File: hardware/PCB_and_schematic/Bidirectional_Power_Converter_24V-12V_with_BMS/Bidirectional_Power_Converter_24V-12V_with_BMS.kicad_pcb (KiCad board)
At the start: 2 copper layers, 100 x 100 mm, 8 parts, among them J1 AC_IN, J2 DC_OUT, Q1 IRF540N, Q2 IRF540N, Q3 IRF540N, Q4 IRF540N, U1 LT4320xDD-1

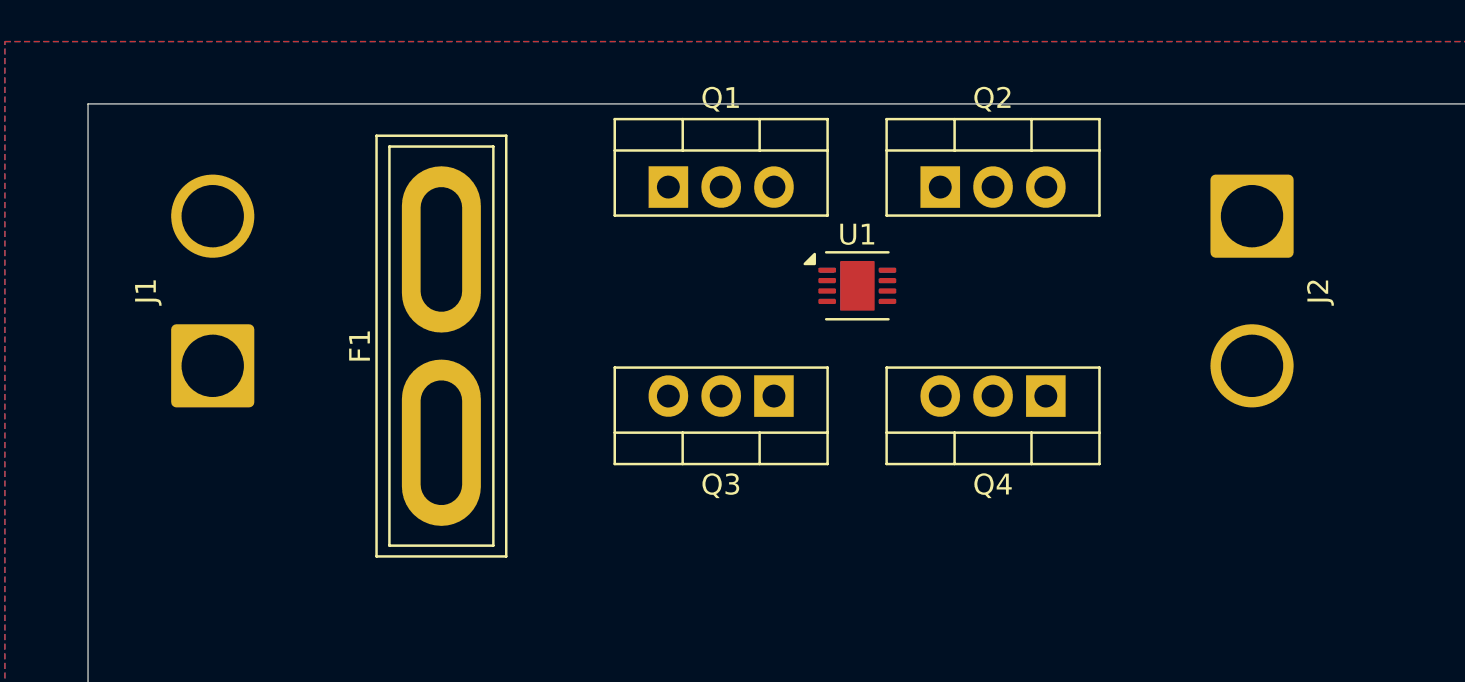
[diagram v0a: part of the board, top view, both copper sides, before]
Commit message: Drawning schematic for buck/boost converter
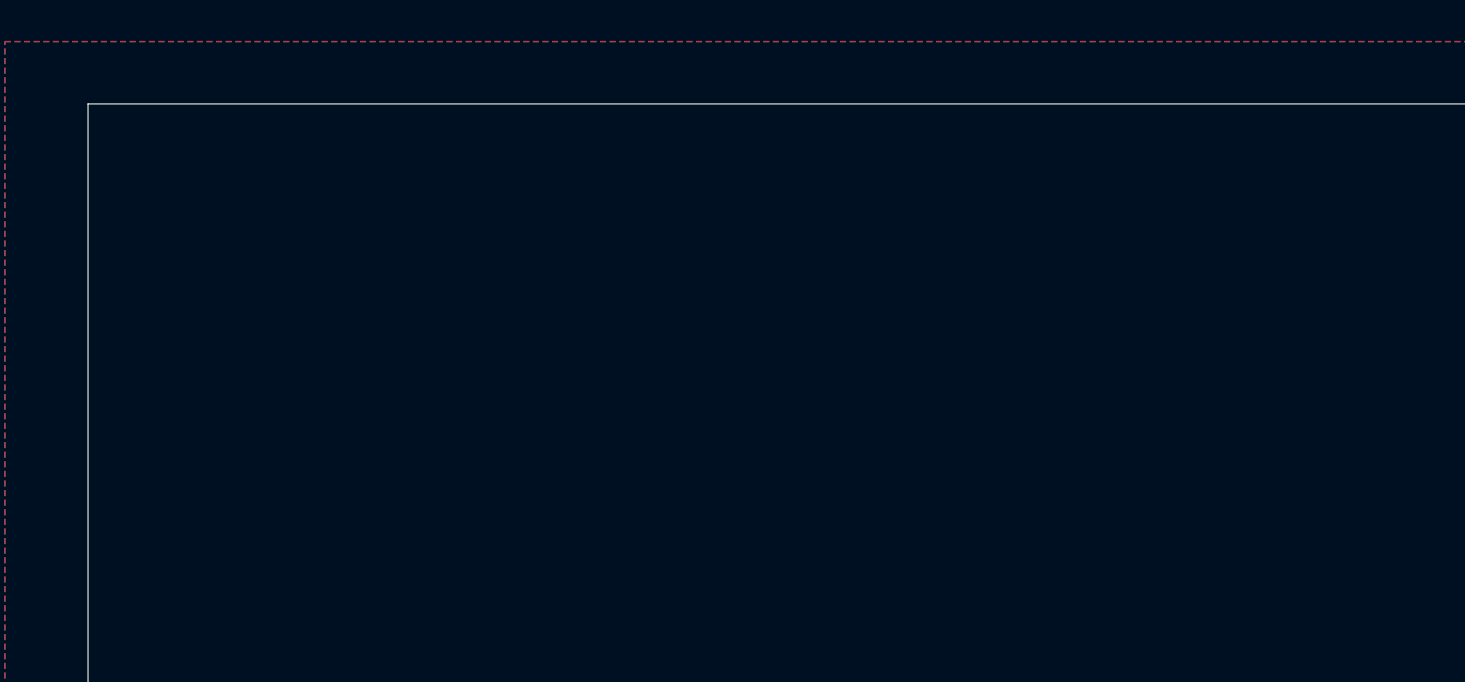
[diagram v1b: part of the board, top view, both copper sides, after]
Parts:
- removed F1: 20A, Fuse:Fuse_Blade_ATO_directSolder
- removed J1: AC_IN, Connector_Wire:SolderWire-2.5sqmm_1x02_P7.2mm_D2.4mm_OD3.6mm
- removed J2: DC_OUT, Connector_Wire:SolderWire-2.5sqmm_1x02_P7.2mm_D2.4mm_OD3.6mm
- removed Q1, Q2, Q3, Q4: IRF540N, Package_TO_SOT_THT:TO-220-3_Vertical
- removed U1: LT4320xDD-1, Package_DFN_QFN:DFN-8-1EP_3x3mm_P0.5mm_EP1.65x2.38mm

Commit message: buck boost progress
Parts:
- added C1: 100n, Resistor_SMD:R_0805_2012Metric_Pad1.20x1.40mm_HandSolder, F.Cu at (57.3, 77.3)
- added C10: 1u, Capacitor_SMD:C_0805_2012Metric_Pad1.18x1.45mm_HandSolder, F.Cu at (58.4, 17.0)
- added C11: 100n, Capacitor_SMD:C_0805_2012Metric_Pad1.18x1.45mm_HandSolder, F.Cu at (58.4, 20.0)
- added C12: 470u/35V, Capacitor_THT:CP_Radial_D8.0mm_P3.50mm, F.Cu at (51.9, 42.9)
- added C13: 100n, Capacitor_SMD:C_0805_2012Metric_Pad1.18x1.45mm_HandSolder, F.Cu at (58.4, 23.0)
- added C14: 100n, Capacitor_SMD:C_0805_2012Metric_Pad1.18x1.45mm_HandSolder, F.Cu at (58.4, 26.0)
- added C15: 22u/6,3V, Capacitor_THT:CP_Radial_D5.0mm_P2.00mm, F.Cu at (51.7, 18.7)
- added C16: 100n, Capacitor_SMD:C_0805_2012Metric_Pad1.18x1.45mm_HandSolder, F.Cu at (58.4, 29.0)
- added C17: 100u/10V, Capacitor_THT:CP_Radial_D8.0mm_P3.50mm, F.Cu at (51.9, 52.4)
- added C18: 10u/10V, Capacitor_THT:CP_Radial_D5.0mm_P2.00mm, F.Cu at (51.7, 25.3)
- added C19: 22u/6,3V, Capacitor_THT:CP_Radial_D5.0mm_P2.00mm, F.Cu at (51.7, 31.8)
- added C2: 100n, Resistor_SMD:R_0805_2012Metric_Pad1.20x1.40mm_HandSolder, F.Cu at (57.3, 80.2)
- added C20: 100n, Capacitor_SMD:C_0805_2012Metric_Pad1.18x1.45mm_HandSolder, F.Cu at (58.4, 32.0)
- added C21: 100n, Capacitor_SMD:C_0805_2012Metric_Pad1.18x1.45mm_HandSolder, F.Cu at (58.4, 35.0)
- added C22: 100n, Resistor_SMD:R_0805_2012Metric_Pad1.20x1.40mm_HandSolder, F.Cu at (14.2, 39.6)
- added C23: 100n, Resistor_SMD:R_0805_2012Metric_Pad1.20x1.40mm_HandSolder, F.Cu at (14.2, 42.5)
- added C3: 1n, Capacitor_SMD:C_0805_2012Metric_Pad1.18x1.45mm_HandSolder, F.Cu at (57.4, 83.2)
- added C4: 1000u/35V, Capacitor_THT:CP_Radial_D10.0mm_P3.50mm, F.Cu at (22.6, 81.6)
- added C5: 1000u/35V, Capacitor_THT:CP_Radial_D10.0mm_P3.50mm, F.Cu at (22.6, 93.2)
- added C6: 100n, Resistor_SMD:R_0805_2012Metric_Pad1.20x1.40mm_HandSolder, F.Cu at (107.8, 77.3)
- added C7: 2.2n, Capacitor_SMD:C_0805_2012Metric_Pad1.18x1.45mm_HandSolder, F.Cu at (101.0, 120.2)
- added C8: 1000u/35V, Capacitor_THT:CP_Radial_D10.0mm_P3.50mm, F.Cu at (73.1, 81.6)
- added C9: 1000u/35V, Capacitor_THT:CP_Radial_D10.0mm_P3.50mm, F.Cu at (73.1, 93.2)
- added D1: 3V3, Diode_SMD:D_MiniMELF, F.Cu at (98.6, 44.9)
- added D10: LED, LED_THT:LED_D5.0mm, F.Cu at (14.3, 19.2)
- added D11: LED, LED_THT:LED_D5.0mm, F.Cu at (21.8, 19.2)
- added D12: LED, LED_THT:LED_D5.0mm, F.Cu at (29.3, 19.2)
- added D13: LED, LED_THT:LED_D5.0mm, F.Cu at (36.8, 19.2)
- added D14: LED, LED_THT:LED_D5.0mm, F.Cu at (44.3, 19.2)
- added D15: LED, LED_THT:LED_D5.0mm, F.Cu at (14.3, 26.8)
- added D16: LED, LED_THT:LED_D5.0mm, F.Cu at (21.8, 26.8)
- added D17: LED, LED_THT:LED_D5.0mm, F.Cu at (29.3, 26.8)
- added D18: D_TVS, Diode_SMD:D_SMC, F.Cu at (63.8, 42.0)
- added D19: D_TVS, Diode_SMD:D_SMC, F.Cu at (63.8, 49.7)
- added D2: 3V3, Diode_SMD:D_MiniMELF, F.Cu at (44.9, 111.8)
- added D20: 3V3, Diode_SMD:D_MiniMELF, F.Cu at (26.6, 66.3)
- added D21: 3V3, Diode_SMD:D_MiniMELF, F.Cu at (26.6, 69.7)
- added D22: LED, LED_THT:LED_D5.0mm, F.Cu at (36.8, 26.8)
- added D23: LED, LED_THT:LED_D5.0mm, F.Cu at (44.3, 26.8)
- added D24: LED, LED_THT:LED_D5.0mm, F.Cu at (14.3, 34.3)
- added D25: LED, LED_THT:LED_D5.0mm, F.Cu at (21.8, 34.3)
- added D26: LED, LED_THT:LED_D5.0mm, F.Cu at (29.3, 34.3)
- added D27: LED, LED_THT:LED_D5.0mm, F.Cu at (36.8, 34.3)
- added D3: D_Schottky, Diode_SMD:D_MiniMELF, F.Cu at (44.9, 115.1)
- added D4: LL4148, Diode_SMD:D_MiniMELF, F.Cu at (44.9, 118.5)
- added D5: D_Schottky_Dua, My-Footprints:TO-220-3_Vertical-little-bigger pads, F.Cu at (33.4, 114.0)
- added D6: 3V3, Diode_SMD:D_MiniMELF, F.Cu at (95.4, 111.8)
- added D7: D_Schottky, Diode_SMD:D_MiniMELF, F.Cu at (95.4, 115.1)
- added D8: LL4148, Diode_SMD:D_MiniMELF, F.Cu at (95.4, 118.5)
- added D9: D_Schottky_Dua, My-Footprints:TO-220-3_Vertical-little-bigger pads, F.Cu at (83.9, 114.0)
- added F1: Fuse, My-Footprints:Fuseholder_Clip-5x20mm_Eaton_1A5601-01_Inline_P20.80x6.76mm_D1.70mm_Horizontal, F.Cu at (74.6, 19.4)
- added F2: Fuse, My-Footprints:Fuseholder_Clip-5x20mm_Eaton_1A5601-01_Inline_P20.80x6.76mm_D1.70mm_Horizontal, F.Cu at (74.6, 27.4)
- added J1: V_IN, My-Footprints-connectors:Flat-6,3mm-connector-4P, F.Cu at (72.8, 32.2)
- added J2: V_OUT, My-Footprints-connectors:Flat-6,3mm-connector-4P, F.Cu at (72.8, 48.5)
- added J3: ICP, Connector_PinHeader_2.54mm:PinHeader_1x06_P2.54mm_Vertical, F.Cu at (63.1, 17.8)
- added J4: RS485, Connector_PinHeader_2.54mm:PinHeader_1x04_P2.54mm_Vertical, F.Cu at (67.8, 17.8)
- added J5: TEMP_BATT, Connector_JST:JST_EH_B3B-EH-A_1x03_P2.50mm_Vertical, F.Cu at (52.2, 59.8)
- added J6: TEMP_BUCK, Connector_JST:JST_EH_B3B-EH-A_1x03_P2.50mm_Vertical, F.Cu at (52.2, 65.7)
- added L1: 60uH (100kHz), Inductor_THT:L_Toroid_Vertical_L28.6mm_W14.3mm_P11.43mm_Bourns_5700, F.Cu at (45.2, 96.1)
- added L2: L, Inductor_THT:L_Toroid_Vertical_L28.6mm_W14.3mm_P11.43mm_Bourns_5700, F.Cu at (95.7, 96.1)
- added Q1: BC337, Package_TO_SOT_THT:TO-92_Inline, F.Cu at (13.8, 79.1)
- added Q10: PMOS, My-Footprints:TO-220-3_Vertical-little-bigger pads, F.Cu at (83.9, 120.0)
- added Q11: BC817, Package_TO_SOT_SMD:SOT-23, F.Cu at (33.3, 40.5)
- added Q12: BC807, Package_TO_SOT_SMD:SOT-23, F.Cu at (33.3, 45.1)
- added Q13: BC817, Package_TO_SOT_SMD:SOT-23, F.Cu at (33.3, 49.8)
- added Q14: BC817, Package_TO_SOT_SMD:SOT-23, F.Cu at (33.3, 54.4)
- added Q15: BC817, Package_TO_SOT_SMD:SOT-23, F.Cu at (33.3, 59.0)
- added Q16: BC807, Package_TO_SOT_SMD:SOT-23, F.Cu at (33.3, 63.6)
- added Q2: BC337, Package_TO_SOT_THT:TO-92_Inline, F.Cu at (13.8, 84.9)
- added Q3: BC337, Package_TO_SOT_THT:TO-92_Inline, F.Cu at (13.8, 90.7)
- added Q4: BC327, Package_TO_SOT_THT:TO-92_Inline, F.Cu at (13.8, 96.5)
- added Q5: IRF540N, Package_TO_SOT_THT:TO-220-3_Vertical, F.Cu at (33.4, 120.0)
- added Q6: BC337, Package_TO_SOT_THT:TO-92_Inline, F.Cu at (64.3, 79.1)
- added Q7: BC337, Package_TO_SOT_THT:TO-92_Inline, F.Cu at (64.3, 84.9)
- added Q8: BC337, Package_TO_SOT_THT:TO-92_Inline, F.Cu at (64.3, 90.7)
- added Q9: BC327, Package_TO_SOT_THT:TO-92_Inline, F.Cu at (64.3, 96.5)
- added R1: 10k, Resistor_SMD:R_0805_2012Metric, F.Cu at (97.6, 32.9)
- added R10: 100mR, Resistor_SMD:R_0805_2012Metric, F.Cu at (106.5, 35.9)
- added R11: R, Resistor_SMD:R_0805_2012Metric, F.Cu at (106.5, 38.8)
- added R12: R, Resistor_SMD:R_0805_2012Metric, F.Cu at (106.5, 41.8)
- added R13: R, Resistor_SMD:R_0805_2012Metric, F.Cu at (32.4, 77.3)
- added R14: R, Resistor_SMD:R_0805_2012Metric, F.Cu at (32.4, 80.2)
- added R15: 6k8, Resistor_SMD:R_0805_2012Metric, F.Cu at (32.4, 83.2)
- added R16: 4k7, Resistor_SMD:R_0805_2012Metric, F.Cu at (32.4, 86.2)
- added R17: 10k, Resistor_SMD:R_0805_2012Metric, F.Cu at (32.4, 89.1)
- added R18: 1k, Resistor_SMD:R_0805_2012Metric, F.Cu at (32.4, 92.0)
- added R19: 10k, Resistor_SMD:R_0805_2012Metric, F.Cu at (36.8, 77.3)
- added R2: R, Resistor_SMD:R_0805_2012Metric, F.Cu at (97.6, 35.9)
- added R20: 470R, Resistor_SMD:R_0805_2012Metric, F.Cu at (36.8, 80.2)
- added R21: 4.7k, Resistor_SMD:R_0805_2012Metric, F.Cu at (36.8, 83.2)
- added R22: 47k, Resistor_SMD:R_0805_2012Metric, F.Cu at (36.8, 86.2)
- added R23: R, Resistor_SMD:R_0805_2012Metric, F.Cu at (36.8, 89.1)
- added R24: 0R, Resistor_SMD:R_0805_2012Metric, F.Cu at (36.8, 92.0)
- added R25: 10k, Resistor_SMD:R_0805_2012Metric, F.Cu at (41.2, 77.3)
- added R26: 1k, Resistor_SMD:R_0805_2012Metric, F.Cu at (41.2, 80.2)
- added R27: R, Resistor_SMD:R_0805_2012Metric, F.Cu at (41.2, 83.2)
- added R28: R, Resistor_SMD:R_0805_2012Metric, F.Cu at (82.8, 77.3)
- added R29: 6k8, Resistor_SMD:R_0805_2012Metric, F.Cu at (82.8, 80.2)
- added R3: 100mR, Resistor_SMD:R_0805_2012Metric, F.Cu at (97.6, 38.8)
- added R30: 4k7, Resistor_SMD:R_0805_2012Metric, F.Cu at (82.8, 83.2)
- added R31: R, Resistor_SMD:R_0805_2012Metric, F.Cu at (82.8, 86.2)
- added R32: 10k, Resistor_SMD:R_0805_2012Metric, F.Cu at (82.8, 89.1)
- added R33: 10k, Resistor_SMD:R_0805_2012Metric, F.Cu at (82.8, 92.0)
- added R34: 470R, Resistor_SMD:R_0805_2012Metric, F.Cu at (87.2, 77.3)
- added R35: 1k, Resistor_SMD:R_0805_2012Metric, F.Cu at (87.2, 80.2)
- added R36: R, Resistor_SMD:R_0805_2012Metric, F.Cu at (87.2, 83.2)
- added R37: 47k, Resistor_SMD:R_0805_2012Metric, F.Cu at (87.2, 86.2)
- added R38: R, Resistor_SMD:R_0805_2012Metric, F.Cu at (87.2, 89.1)
- added R39: 0R, Resistor_SMD:R_0805_2012Metric, F.Cu at (87.2, 92.0)
- added R4: R, Resistor_SMD:R_0805_2012Metric, F.Cu at (97.6, 41.8)
- added R40: 10k, Resistor_SMD:R_0805_2012Metric, F.Cu at (91.7, 77.3)
- added R41: 1k, Resistor_SMD:R_0805_2012Metric, F.Cu at (91.7, 80.2)
- added R42: R, Resistor_SMD:R_0805_2012Metric, F.Cu at (91.7, 83.2)
- added R43: 120R, Resistor_SMD:R_0805_2012Metric_Pad1.20x1.40mm_HandSolder, F.Cu at (14.2, 45.5)
- added R44: 120R, Resistor_SMD:R_0805_2012Metric_Pad1.20x1.40mm_HandSolder, F.Cu at (14.2, 48.4)
- added R45: 120R, Resistor_SMD:R_0805_2012Metric_Pad1.20x1.40mm_HandSolder, F.Cu at (14.2, 51.4)
- added R46: 120R, Resistor_SMD:R_0805_2012Metric_Pad1.20x1.40mm_HandSolder, F.Cu at (14.2, 54.3)
- added R47: 120R, Resistor_SMD:R_0805_2012Metric_Pad1.20x1.40mm_HandSolder, F.Cu at (14.2, 57.3)
- added R48: 120R, Resistor_SMD:R_0805_2012Metric_Pad1.20x1.40mm_HandSolder, F.Cu at (14.2, 60.2)
- added R49: 120R, Resistor_SMD:R_0805_2012Metric_Pad1.20x1.40mm_HandSolder, F.Cu at (14.2, 63.2)
- added R5: R, Resistor_SMD:R_0805_2012Metric, F.Cu at (102.0, 32.9)
- added R50: 120R, Resistor_SMD:R_0805_2012Metric_Pad1.20x1.40mm_HandSolder, F.Cu at (19.0, 39.6)
- added R51: 1k, Resistor_SMD:R_0805_2012Metric, F.Cu at (67.6, 29.2)
- added R52: 10k, Resistor_SMD:R_0805_2012Metric_Pad1.20x1.40mm_HandSolder, F.Cu at (19.0, 42.5)
- added R53: 510R, Resistor_SMD:R_0805_2012Metric_Pad1.20x1.40mm_HandSolder, F.Cu at (19.0, 45.5)
- added R54: 120R, Resistor_SMD:R_0805_2012Metric_Pad1.20x1.40mm_HandSolder, F.Cu at (19.0, 48.4)
- added R55: 510R, Resistor_SMD:R_0805_2012Metric_Pad1.20x1.40mm_HandSolder, F.Cu at (19.0, 51.4)
- added R56: 10k, Resistor_SMD:R_0805_2012Metric_Pad1.20x1.40mm_HandSolder, F.Cu at (19.0, 54.3)
- added R57: 10k, Resistor_SMD:R_0805_2012Metric_Pad1.20x1.40mm_HandSolder, F.Cu at (19.0, 57.3)
- added R58: 150k, Resistor_SMD:R_0805_2012Metric_Pad1.20x1.40mm_HandSolder, F.Cu at (19.0, 60.2)
- added R59: 150k, Resistor_SMD:R_0805_2012Metric_Pad1.20x1.40mm_HandSolder, F.Cu at (19.0, 63.2)
- added R6: 100mR, Resistor_SMD:R_0805_2012Metric, F.Cu at (102.0, 35.9)
- added R60: 1k, Resistor_SMD:R_0805_2012Metric_Pad1.20x1.40mm_HandSolder, F.Cu at (23.7, 39.6)
- added R61: 1k, Resistor_SMD:R_0805_2012Metric_Pad1.20x1.40mm_HandSolder, F.Cu at (23.7, 42.5)
- added R62: 10K, Resistor_SMD:R_0805_2012Metric_Pad1.20x1.40mm_HandSolder, F.Cu at (23.7, 45.5)
- added R63: 10K, Resistor_SMD:R_0805_2012Metric_Pad1.20x1.40mm_HandSolder, F.Cu at (23.7, 48.4)
- added R64: 10K, Resistor_SMD:R_0805_2012Metric_Pad1.20x1.40mm_HandSolder, F.Cu at (23.7, 51.4)
- added R65: 220R, Resistor_SMD:R_0805_2012Metric_Pad1.20x1.40mm_HandSolder, F.Cu at (23.7, 54.3)
- added R66: 220R, Resistor_SMD:R_0805_2012Metric_Pad1.20x1.40mm_HandSolder, F.Cu at (23.7, 57.3)
- added R67: 220R, Resistor_SMD:R_0805_2012Metric_Pad1.20x1.40mm_HandSolder, F.Cu at (23.7, 60.2)
- added R68: 10K, Resistor_SMD:R_0805_2012Metric_Pad1.20x1.40mm_HandSolder, F.Cu at (23.7, 63.2)
- added R69: 10K, Resistor_SMD:R_0805_2012Metric_Pad1.20x1.40mm_HandSolder, F.Cu at (28.5, 39.6)
- added R7: 100mR, Resistor_SMD:R_0805_2012Metric, F.Cu at (102.0, 38.8)
- added R70: 220R, Resistor_SMD:R_0805_2012Metric_Pad1.20x1.40mm_HandSolder, F.Cu at (28.5, 42.5)
- added R71: 220R, Resistor_SMD:R_0805_2012Metric_Pad1.20x1.40mm_HandSolder, F.Cu at (28.5, 45.5)
- added R72: 10K, Resistor_SMD:R_0805_2012Metric_Pad1.20x1.40mm_HandSolder, F.Cu at (28.5, 48.4)
- added R73: 220R, Resistor_SMD:R_0805_2012Metric_Pad1.20x1.40mm_HandSolder, F.Cu at (28.5, 51.4)
- added R8: R, Resistor_SMD:R_0805_2012Metric, F.Cu at (102.0, 41.8)
- added R9: R, Resistor_SMD:R_0805_2012Metric, F.Cu at (106.5, 32.9)
- added RV1: 10K, Potentiometer_THT:Potentiometer_Runtron_RM-065_Vertical, F.Cu at (49.6, 112.2)
- added RV2: 10K, Potentiometer_THT:Potentiometer_Runtron_RM-065_Vertical, F.Cu at (100.1, 112.2)
- added U1: LM358, Package_DIP:CERDIP-8_W7.62mm_SideBrazed_LongPads, F.Cu at (45.4, 79.4)
- added U10: INA226, Package_SO:VSSOP-10_3x3mm_P0.5mm, F.Cu at (64.5, 35.1)
- added U11: LM358, Package_DIP:CERDIP-8_W7.62mm_SideBrazed_LongPads, F.Cu at (-6.10, 50.0)
- added U2: TL494, Package_DIP:CERDIP-16_W7.62mm_SideBrazed_LongPads, F.Cu at (20.3, 101.0)
- added U4: TL494, Package_DIP:CERDIP-16_W7.62mm_SideBrazed_LongPads, F.Cu at (70.8, 101.0)
- added U5: LM7805_TO220, Package_TO_SOT_THT:TO-220-3_Vertical, F.Cu at (15.1, 68.6)
- added U6: PIC16F886-IP, Package_SO:SOIC-28W_7.5x17.9mm_P1.27mm, F.Cu at (42.6, 46.8)
- added U7: ICL7660, Package_SO:SOIC-8_3.9x4.9mm_P1.27mm, F.Cu at (64.9, 60.6)
- added U8: TL431LP, Package_TO_SOT_THT:TO-92_Inline, F.Cu at (37.7, 71.3)
- added U9: ST485, Package_SO:SOIC-8_3.9x4.9mm_P1.27mm, F.Cu at (64.9, 67.1)
